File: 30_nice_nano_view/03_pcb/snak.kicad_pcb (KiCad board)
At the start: 2 copper layers, 114 x 99 mm, 162 parts

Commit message: update
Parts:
- removed the REF** at (107.8, 79.2)
- removed the REF** at (163.2, 69.2)
- removed the REF** at (178.4, 102.6)
- removed the REF** at (163.2, 51.7)
- removed the REF** at (181.8, 77.2)
- removed the REF** at (181.8, 59.7)
- removed the REF** at (179.4, 114.1)
- removed the REF** at (197.8, 123.0)
- removed the REF** at (104.8, 84.0)
- removed the REF** at (104.8, 66.5)
- removed the REF** at (123.2, 90.2)
- removed the REF** at (123.2, 72.8)
- removed the REF** at (107.8, 61.8)
- removed the REF** at (123.2, 55.2)
- removed the REF** at (141.8, 84.2)
- removed the REF** at (141.8, 66.8)
- removed the REF** at (141.8, 49.2)
- removed the REF** at (160.2, 91.5)
- removed the REF** at (160.2, 74.0)
- removed the REF** at (160.2, 56.5)
- removed the REF** at (178.8, 82.0)
- removed the REF** at (178.8, 64.5)
- removed the REF** at (175.2, 117.8)
- removed the REF** at (126.2, 85.5)
- removed the REF** at (193.0, 125.9)
- removed the REF** at (92.2, 79.2)
- removed the REF** at (92.2, 61.8)
- removed the REF** at (110.8, 85.5)
- removed the REF** at (110.8, 68.0)
- removed the REF** at (110.8, 50.5)
- removed the REF** at (129.2, 79.5)
- removed the REF** at (129.2, 62.0)
- removed the REF** at (129.2, 44.5)
- removed the REF** at (147.8, 86.7)
- removed the REF** at (126.2, 68.0)
- removed the REF** at (147.8, 69.2)
- removed the REF** at (147.8, 51.7)
- removed the REF** at (166.2, 77.2)
- removed the REF** at (166.2, 59.7)
- removed the REF** at (164.6, 109.6)
- removed the REF** at (184.0, 116.0)
- removed the REF** at (95.2, 84.0)
- removed the REF** at (95.2, 66.5)
- removed the REF** at (113.8, 90.2)
- removed the REF** at (113.8, 72.8)
- removed the REF** at (126.2, 50.5)
- removed the REF** at (113.8, 55.2)
- removed the REF** at (132.2, 84.2)
- removed the REF** at (132.2, 66.8)
- removed the REF** at (132.2, 49.2)
- removed the REF** at (150.8, 91.5)
- removed the REF** at (150.8, 74.0)
- removed the REF** at (150.8, 56.5)
- removed the REF** at (169.2, 82.0)
- removed the REF** at (169.2, 64.5)
- removed the REF** at (166.1, 115.0)
- removed the REF** at (144.8, 79.5)
- removed the REF** at (184.5, 121.6)
- removed the REF** at (144.8, 62.0)
- removed the REF** at (144.8, 44.5)
- removed the REF** at (163.2, 86.7)
- removed the REF** at (178.4, 96.4)
- added REF**: VIA-0.6mm, VIA-0.6mm, F.Cu at (107.8, 78.0)
- added REF**: VIA-0.6mm, VIA-0.6mm, F.Cu at (163.2, 68.0)
- added REF**: VIA-0.6mm, VIA-0.6mm, F.Cu at (179.6, 89.5)
- added REF**: VIA-0.6mm, VIA-0.6mm, F.Cu at (163.2, 50.5)
- added REF**: VIA-0.6mm, VIA-0.6mm, F.Cu at (181.8, 76.0)
- added REF**: VIA-0.6mm, VIA-0.6mm, F.Cu at (181.8, 58.5)
- added REF**: VIA-0.6mm, VIA-0.6mm, F.Cu at (179.8, 112.9)
- added REF**: VIA-0.6mm, VIA-0.6mm, F.Cu at (198.4, 121.9)
- added REF**: VIA-0.6mm, VIA-0.6mm, F.Cu at (103.5, 84.0)
- added REF**: VIA-0.6mm, VIA-0.6mm, F.Cu at (103.5, 66.5)
- added REF**: VIA-0.6mm, VIA-0.6mm, F.Cu at (122.0, 90.2)
- added REF**: VIA-0.6mm, VIA-0.6mm, F.Cu at (122.0, 72.8)
- added REF**: VIA-0.6mm, VIA-0.6mm, F.Cu at (107.8, 60.5)
- added REF**: VIA-0.6mm, VIA-0.6mm, F.Cu at (122.0, 55.2)
- added REF**: VIA-0.6mm, VIA-0.6mm, F.Cu at (140.5, 84.2)
- added REF**: VIA-0.6mm, VIA-0.6mm, F.Cu at (140.5, 66.8)
- added REF**: VIA-0.6mm, VIA-0.6mm, F.Cu at (140.5, 49.2)
- added REF**: VIA-0.6mm, VIA-0.6mm, F.Cu at (159.0, 91.5)
- added REF**: VIA-0.6mm, VIA-0.6mm, F.Cu at (159.0, 74.0)
- added REF**: VIA-0.6mm, VIA-0.6mm, F.Cu at (159.0, 56.5)
- added REF**: VIA-0.6mm, VIA-0.6mm, F.Cu at (177.5, 82.0)
- added REF**: VIA-0.6mm, VIA-0.6mm, F.Cu at (177.5, 64.5)
- added REF**: VIA-0.6mm, VIA-0.6mm, F.Cu at (174.0, 117.4)
- added REF**: VIA-0.6mm, VIA-0.6mm, F.Cu at (126.2, 84.2)
- added REF**: VIA-0.6mm, VIA-0.6mm, F.Cu at (191.9, 125.3)
- added REF**: VIA-0.6mm, VIA-0.6mm, F.Cu at (92.2, 78.0)
- added REF**: VIA-0.6mm, VIA-0.6mm, F.Cu at (92.2, 60.5)
- added REF**: VIA-0.6mm, VIA-0.6mm, F.Cu at (110.8, 84.2)
- added REF**: VIA-0.6mm, VIA-0.6mm, F.Cu at (110.8, 66.8)
- added REF**: VIA-0.6mm, VIA-0.6mm, F.Cu at (110.8, 49.2)
- added REF**: VIA-0.6mm, VIA-0.6mm, F.Cu at (129.2, 78.2)
- added REF**: VIA-0.6mm, VIA-0.6mm, F.Cu at (129.2, 60.8)
- added REF**: VIA-0.6mm, VIA-0.6mm, F.Cu at (129.2, 43.2)
- added REF**: VIA-0.6mm, VIA-0.6mm, F.Cu at (147.8, 85.5)
- added REF**: VIA-0.6mm, VIA-0.6mm, F.Cu at (126.2, 66.8)
- added REF**: VIA-0.6mm, VIA-0.6mm, F.Cu at (147.8, 68.0)
- added REF**: VIA-0.6mm, VIA-0.6mm, F.Cu at (147.8, 50.5)
- added REF**: VIA-0.6mm, VIA-0.6mm, F.Cu at (166.2, 76.0)
- added REF**: VIA-0.6mm, VIA-0.6mm, F.Cu at (166.2, 58.5)
- added REF**: VIA-0.6mm, VIA-0.6mm, F.Cu at (165.0, 108.4)
- added REF**: VIA-0.6mm, VIA-0.6mm, F.Cu at (184.6, 114.9)
- added REF**: VIA-0.6mm, VIA-0.6mm, F.Cu at (96.5, 84.0)
- added REF**: VIA-0.6mm, VIA-0.6mm, F.Cu at (96.5, 66.5)
- added REF**: VIA-0.6mm, VIA-0.6mm, F.Cu at (115.0, 90.2)
- added REF**: VIA-0.6mm, VIA-0.6mm, F.Cu at (115.0, 72.8)
- added REF**: VIA-0.6mm, VIA-0.6mm, F.Cu at (126.2, 49.2)
- added REF**: VIA-0.6mm, VIA-0.6mm, F.Cu at (115.0, 55.2)
- added REF**: VIA-0.6mm, VIA-0.6mm, F.Cu at (133.5, 84.2)
- added REF**: VIA-0.6mm, VIA-0.6mm, F.Cu at (133.5, 66.8)
- added REF**: VIA-0.6mm, VIA-0.6mm, F.Cu at (133.5, 49.2)
- added REF**: VIA-0.6mm, VIA-0.6mm, F.Cu at (152.0, 91.5)
- added REF**: VIA-0.6mm, VIA-0.6mm, F.Cu at (152.0, 74.0)
- added REF**: VIA-0.6mm, VIA-0.6mm, F.Cu at (152.0, 56.5)
- added REF**: VIA-0.6mm, VIA-0.6mm, F.Cu at (170.5, 82.0)
- added REF**: VIA-0.6mm, VIA-0.6mm, F.Cu at (170.5, 64.5)
- added REF**: VIA-0.6mm, VIA-0.6mm, F.Cu at (167.3, 115.4)
- added REF**: VIA-0.6mm, VIA-0.6mm, F.Cu at (144.8, 78.2)
- added REF**: VIA-0.6mm, VIA-0.6mm, F.Cu at (185.6, 122.1)
- added REF**: VIA-0.6mm, VIA-0.6mm, F.Cu at (144.8, 60.8)
- added REF**: VIA-0.6mm, VIA-0.6mm, F.Cu at (144.8, 43.2)
- added REF**: VIA-0.6mm, VIA-0.6mm, F.Cu at (163.2, 85.5)
- added REF**: VIA-0.6mm, VIA-0.6mm, F.Cu at (179.6, 95.7)
- moved JST1 8.57 mm to (179.6, 91.8), turned to 0 degrees
- moved D29 1.35 mm to (163.6, 111.1)
- moved D15 1.35 mm to (197.5, 124.8)
- moved D14 1.35 mm to (179.4, 115.9)
- moved D1 1.35 mm to (108.2, 81.0)
- moved D10 1.35 mm to (163.8, 71.0)
- moved D11 1.35 mm to (163.8, 53.5)
- moved D12 1.35 mm to (182.2, 79.0)
- moved D13 1.35 mm to (182.2, 61.5)
- moved D16 1.35 mm to (91.8, 81.0)
- moved D17 1.35 mm to (91.8, 63.5)
- moved D18 1.35 mm to (110.2, 87.2)
- moved D19 1.35 mm to (110.2, 69.8)
- moved D2 1.35 mm to (108.2, 63.5)
- moved D20 1.35 mm to (110.2, 52.2)
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
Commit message: update
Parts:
- removed the REF** at (179.6, 89.5)
- removed the REF** at (179.8, 112.9)
- removed the REF** at (198.4, 121.9)
- removed the REF** at (174.0, 117.4)
- removed the REF** at (191.9, 125.3)
- removed the REF** at (165.0, 108.4)
- removed the REF** at (184.6, 114.9)
- removed the REF** at (167.3, 115.4)
- removed the REF** at (185.6, 122.1)
- removed the REF** at (170.0, 118.4)
- removed the REF** at (187.8, 125.6)
- removed the REF** at (170.3, 117.3)
- removed the REF** at (188.3, 124.6)
- removed the REF** at (182.7, 112.6)
- removed the REF** at (165.4, 104.3)
- removed the REF** at (185.7, 111.0)
- removed the REF** at (186.9, 97.4)
- removed the REF** at (186.1, 96.7)
- removed the REF** at (185.3, 95.9)
- removed the REF** at (193.7, 97.8)
- removed the REF** at (193.2, 61.0)
- removed the REF** at (179.6, 95.7)
- added REF**: VIA-0.6mm, VIA-0.6mm, F.Cu at (193.2, 55.5)
- added REF**: VIA-0.6mm, VIA-0.6mm, F.Cu at (177.3, 92.3)
- added REF**: VIA-0.6mm, VIA-0.6mm, F.Cu at (182.3, 92.3)
- added REF**: VIA-0.6mm, VIA-0.6mm, F.Cu at (179.8, 113.1)
- added REF**: VIA-0.6mm, VIA-0.6mm, F.Cu at (198.1, 123.3)
- added REF**: VIA-0.6mm, VIA-0.6mm, F.Cu at (173.9, 117.5)
- added REF**: VIA-0.6mm, VIA-0.6mm, F.Cu at (191.4, 126.3)
- added REF**: VIA-0.6mm, VIA-0.6mm, F.Cu at (165.1, 108.3)
- added REF**: VIA-0.6mm, VIA-0.6mm, F.Cu at (184.8, 115.3)
- added REF**: VIA-0.6mm, VIA-0.6mm, F.Cu at (167.3, 115.3)
- added REF**: VIA-0.6mm, VIA-0.6mm, F.Cu at (185.4, 122.7)
- added REF**: VIA-0.6mm, VIA-0.6mm, F.Cu at (169.9, 118.4)
- added REF**: VIA-0.6mm, VIA-0.6mm, F.Cu at (187.3, 126.3)
- added REF**: VIA-0.6mm, VIA-0.6mm, F.Cu at (170.3, 117.3)
- added REF**: VIA-0.6mm, VIA-0.6mm, F.Cu at (187.9, 125.3)
- added REF**: VIA-0.6mm, VIA-0.6mm, F.Cu at (182.8, 112.8)
- added REF**: VIA-0.6mm, VIA-0.6mm, F.Cu at (165.6, 104.2)
- added REF**: VIA-0.6mm, VIA-0.6mm, F.Cu at (186.2, 111.5)
- added REF**: VIA-0.6mm, VIA-0.6mm, F.Cu at (189.2, 89.8)
- added REF**: VIA-0.6mm, VIA-0.6mm, F.Cu at (198.1, 89.8)
- added REF**: VIA-0.6mm, VIA-0.6mm, F.Cu at (193.7, 90.7)
- added REF**: VIA-0.6mm, VIA-0.6mm, F.Cu at (189.8, 90.7)
- added REF**: VIA-0.6mm, VIA-0.6mm, F.Cu at (197.5, 90.7)
- added REF**: VIA-0.6mm, VIA-0.6mm, F.Cu at (193.7, 91.8)
- moved DISP1 7.00 mm to (193.7, 77.2)
- moved H10 5.50 mm to (200.4, 57.0)
- moved MCU1 5.50 mm to (193.7, 73.2)
- moved SW1 5.50 mm to (193.2, 56.6)
- moved JST1 1.49 mm to (180.9, 92.3), turned to 270 degrees
- moved D15 1.43 mm to (197.0, 126.2), turned to 239 degrees
- moved S15 0.85 mm to (189.1, 123.2), turned to 149 degrees
- moved D30 0.35 mm to (182.8, 117.7), turned to 239 degrees
- moved H9 0.23 mm to (177.0, 126.6), turned to -18 degrees
- moved D29 0.15 mm to (163.7, 111.0), turned to 252 degrees
- moved D14 0.15 mm to (179.4, 116.1), turned to 252 degrees
- turned S14 to 162 degrees
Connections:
- MCU1 pad 114: R3 -> CS
- MCU1 pad 115: R2 -> SCK
- MCU1 pad 116: R1 -> MOSI
- MCU1 pad 117: CS -> R3
- MCU1 pad 118: SCK -> R2
- MCU1 pad 119: MOSI -> R1
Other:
- board size 114 x 99 mm -> 114 x 100.2 mm

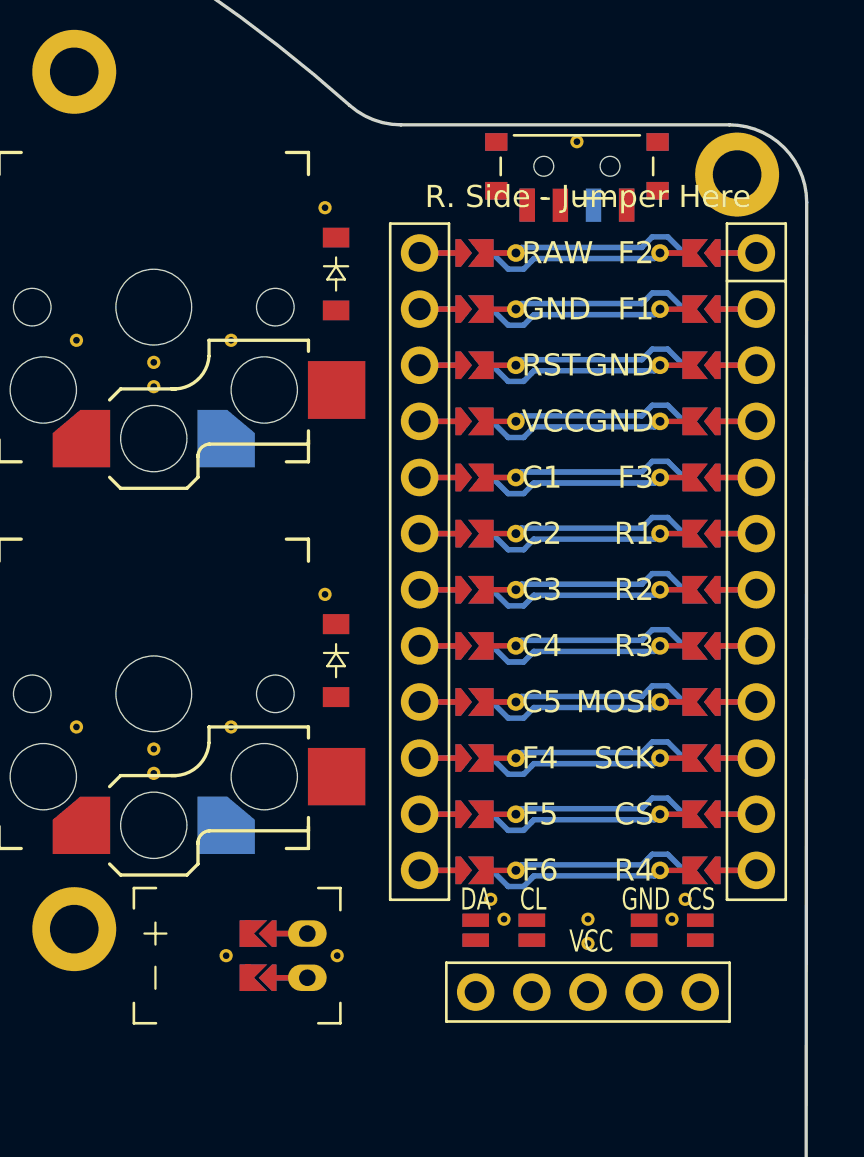
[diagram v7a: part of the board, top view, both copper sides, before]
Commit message: move mcu mount hole further right
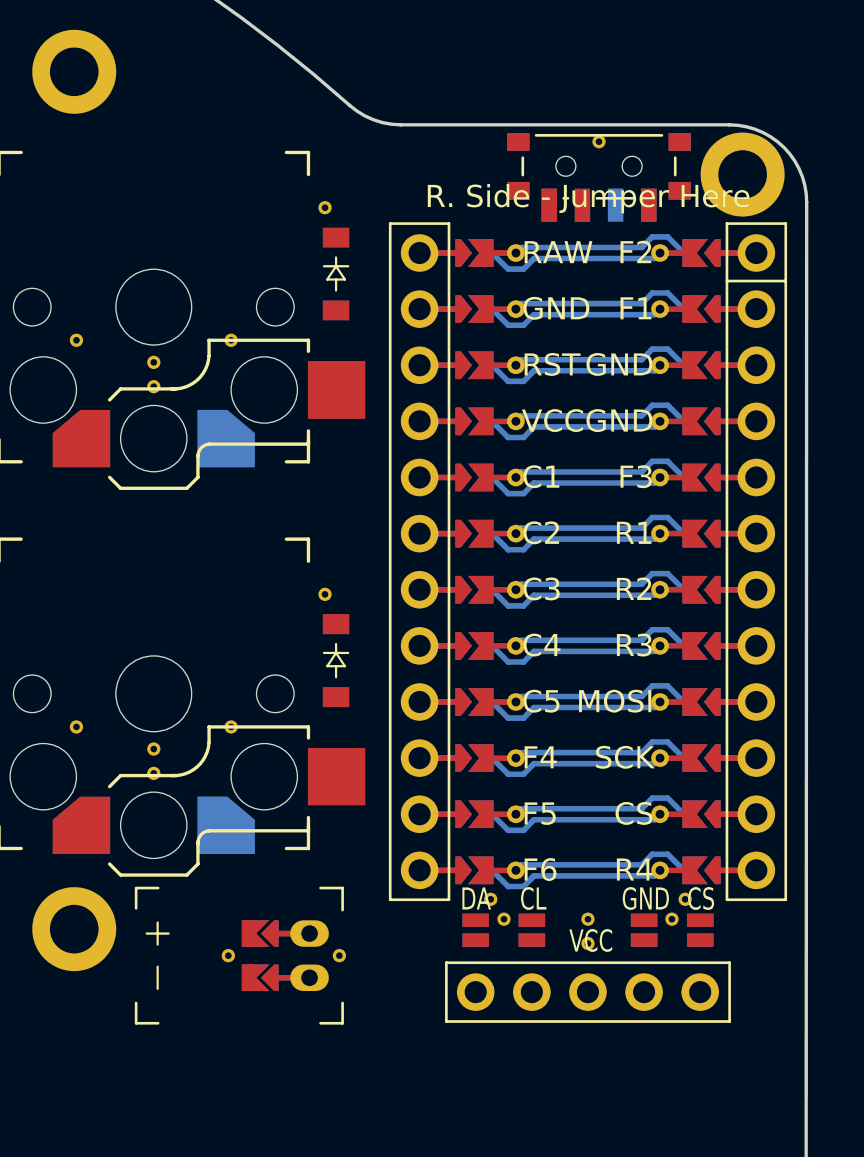
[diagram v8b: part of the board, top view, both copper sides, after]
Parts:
- removed the REF** at (193.2, 55.5)
- removed the REF** at (177.3, 92.3)
- removed the REF** at (182.3, 92.3)
- added REF**: VIA-0.6mm, VIA-0.6mm, F.Cu at (194.2, 55.5)
- added REF**: VIA-0.6mm, VIA-0.6mm, F.Cu at (177.4, 92.3)
- added REF**: VIA-0.6mm, VIA-0.6mm, F.Cu at (182.4, 92.3)
- moved SW1 1.00 mm to (194.2, 56.6)
- moved H10 0.25 mm to (200.7, 57.0)
- moved JST1 0.10 mm to (181.1, 92.3)
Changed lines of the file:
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@@
       )
       (module power_switch (layer F.Cu)
-        (at 193.15 56.6 90)
+        (at 194.15 56.6 90)
         (attr smd)
         (fp_text reference "SW1" (at -3.6 0 0) (layer F.SilkS) hide
@@
       )
       (module VIA-0.6mm (layer F.Cu)
-      (at 193.15 55.4625 90)
+      (at 194.15 55.4625 90)
       (fp_text reference REF** (at 0 1.4) (layer F.SilkS) hide (effects (font (size 1 1) (thickness 0.15))))
       (fp_text value VIA-0.6mm (at 0 -1.4) (layer F.Fab) hide (effects (font (size 1 1) (thickness 0.15))))
@@
       )
             (module "JST_PH_S2B-PH-K" (layer F.Cu)
-                (at 180.95 92.3 270)
+                (at 181.05 92.3 270)
                 (descr "JST PH series connector, S2B-PH-K (http://www.jst-mfg.com/product/pdf/eng/ePH.pdf)")
                 (fp_text reference "JST1" (at 1 -2.55 270) (layer "F.SilkS") hide
@@
                     ) )
             )
-        (segment (start 179.150 91.300) (end 180.950 91.300) (width 0.25) (layer "F.Cu") (net 67))
-        (segment (start 179.150 91.300) (end 180.950 91.300) (width 0.25) (layer "B.Cu") (net 67))
-        (segment (start 179.150 93.300) (end 180.950 93.300) (width 0.25) (layer "F.Cu") (net 68))
-        (segment (start 179.150 93.300) (end 180.950 93.300) (width 0.25) (layer "B.Cu") (net 68))
+        (segment (start 179.250 91.300) (end 181.050 91.300) (width 0.25) (layer "F.Cu") (net 67))
+        (segment (start 179.250 91.300) (end 181.050 91.300) (width 0.25) (layer "B.Cu") (net 67))
+        (segment (start 179.250 93.300) (end 181.050 93.300) (width 0.25) (layer "F.Cu") (net 68))
+        (segment (start 179.250 93.300) (end 181.050 93.300) (width 0.25) (layer "B.Cu") (net 68))
       (module VIA-0.6mm (layer F.Cu)
-      (at 177.27499999999998 92.3 270)
+      (at 177.375 92.3 270)
       (fp_text reference REF** (at 0 1.4) (layer F.SilkS) hide (effects (font (size 1 1) (thickness 0.15))))
       (fp_text value VIA-0.6mm (at 0 -1.4) (layer F.Fab) hide (effects (font (size 1 1) (thickness 0.15))))
@@
       )
       (module VIA-0.6mm (layer F.Cu)
-      (at 182.29999999999998 92.3 270)
+      (at 182.4 92.3 270)
       (fp_text reference REF** (at 0 1.4) (layer F.SilkS) hide (effects (font (size 1 1) (thickness 0.15))))
       (fp_text value VIA-0.6mm (at 0 -1.4) (layer F.Fab) hide (effects (font (size 1 1) (thickness 0.15))))
@@
             )
             (module mounting_hole (layer F.Cu)
-                (at 200.4 56.95 0)
+                (at 200.65 56.95 0)
                 (fp_text reference "H10" (at 0 3) (layer F.SilkS) hide
                     (effects (font (size 1 1) (thickness 0.15)))
@@
 (gr_circle (center 170.4 91.10000000000001) (end 171.4 91.10000000000001) (layer Eco1.User) (width 0.15))
 (gr_circle (center 176.9888656 126.60568) (end 177.9888656 126.60568) (layer Eco1.User) (width 0.15))
-(gr_circle (center 200.4 56.95) (end 201.4 56.95) (layer Eco1.User) (width 0.15))
+(gr_circle (center 200.65 56.95) (end 201.65 56.95) (layer Eco1.User) (width 0.15))
 (gr_line (start 93.05 89.45) (end 106.95 89.45) (angle 90) (layer Eco1.User) (width 0.15))
 (gr_line (start 106.95 89.45) (end 106.95 75.55) (angle 90) (layer Eco1.User) (width 0.15))
@@
 (gr_circle (center 170.4 91.10000000000001) (end 171.9 91.10000000000001) (layer Eco2.User) (width 0.15))
 (gr_circle (center 176.9888656 126.60568) (end 178.4888656 126.60568) (layer Eco2.User) (width 0.15))
-(gr_circle (center 200.4 56.95) (end 201.9 56.95) (layer Eco2.User) (width 0.15))
+(gr_circle (center 200.65 56.95) (end 202.15 56.95) (layer Eco2.User) (width 0.15))
 )
